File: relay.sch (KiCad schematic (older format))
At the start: 0 parts

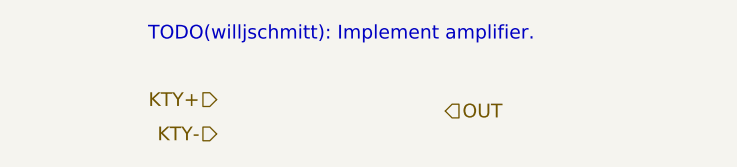
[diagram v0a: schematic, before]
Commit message: Adding contactor placeholders.
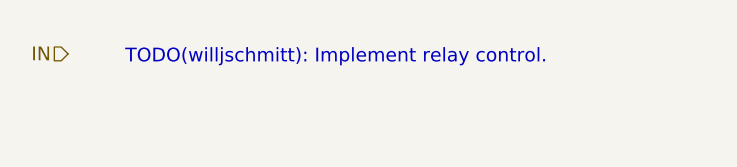
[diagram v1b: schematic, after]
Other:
- note added: "TODO(willjschmitt): Implement relay control."
- note removed: "TODO(willjschmitt): Implement amplifier."
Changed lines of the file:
@@
 $Descr A4 11693 8268
 encoding utf-8
-Sheet 13 18
+Sheet 17 18
 Title ""
 Date ""
@@
 Comment4 ""
 $EndDescr
-Text HLabel 2150 1300 0    60   Input ~ 0
-KTY+
-Text HLabel 2150 1450 0    60   Input ~ 0
-KTY-
-Text HLabel 3150 1350 2    60   Input ~ 0
-OUT
-Text Notes 1850 1050 0    60   ~ 0
-TODO(willjschmitt): Implement amplifier.
+Text HLabel 1500 1100 0    60   Input ~ 0
+IN
+Text Notes 1750 1150 0    60   ~ 0
+TODO(willjschmitt): Implement relay control.
 $EndSCHEMATC

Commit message: Implement contactor relays.
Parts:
- added D? (x2): D, symbol D
- added PRECHARGE: CONN, symbol Conn_01x02
- added Q?: Q_NPN_BCE, symbol Q_NPN_BCE
- added U?: RELAY_SPST, symbol RELAY_SPST
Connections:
- net labels added: +5V, GND
- wire segments 0 -> 16
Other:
- note removed: "TODO(willjschmitt): Implement relay control."
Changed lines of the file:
@@
 $Descr A4 11693 8268
 encoding utf-8
-Sheet 17 18
+Sheet 18 18
 Title ""
 Date ""
@@
 Comment4 ""
 $EndDescr
-Text HLabel 1500 1100 0    60   Input ~ 0
+Text HLabel 5400 4000 0    60   Input ~ 0
 IN
-Text Notes 1750 1150 0    60   ~ 0
-TODO(willjschmitt): Implement relay control.
+$Comp
+L Q_NPN_BCE Q?
+U 1 1 5B006B25
+P 5750 4000
+AR Path="/5AFF2F49/5AFF30F9/5B006B25" Ref="Q?"  Part="1"
+AR Path="/5AFF2F49/5AFF3733/5B006B25" Ref="Q?"  Part="1"
+F 0 "Q?" H 5950 4050 50  0000 L CNN
+F 1 "Q_NPN_BCE" H 5950 3950 50  0000 L CNN
+F 2 "" H 5950 4100 50  0001 C CNN
+F 3 "" H 5750 4000 50  0001 C CNN
+	1    5750 4000
+	1    0    0    -1
+$EndComp
+Wire Wire Line
+	5550 4000 5400 4000
+$Comp
+L RELAY_SPST U?
+U 1 1 5B006EB3
+P 6450 3450
+AR Path="/5AFF2F49/5AFF30F9/5B006EB3" Ref="U?"  Part="1"
+AR Path="/5AFF2F49/5AFF3733/5B006EB3" Ref="U?"  Part="1"
+F 0 "U?" H 6450 3150 60  0000 C CNN
+F 1 "RELAY_SPST" H 6450 3750 60  0000 C CNN
+F 2 "" H 6450 3450 60  0001 C CNN
+F 3 "" H 6450 3450 60  0001 C CNN
+	1    6450 3450
+	1    0    0    -1
+$EndComp
+$Comp
+L +5V #PWR?
+U 1 1 5B006F20
+P 5850 3050
+AR Path="/5AFF2F49/5AFF30F9/5B006F20" Ref="#PWR?"  Part="1"
+AR Path="/5AFF2F49/5AFF3733/5B006F20" Ref="#PWR?"  Part="1"
+F 0 "#PWR?" H 5850 2900 50  0001 C CNN
+F 1 "+5V" H 5850 3190 50  0000 C CNN
+F 2 "" H 5850 3050 50  0001 C CNN
+F 3 "" H 5850 3050 50  0001 C CNN
+	1    5850 3050
+	1    0    0    -1
+$EndComp
+$Comp
+L GND #PWR?
+U 1 1 5B006F38
+P 5850 4300
+AR Path="/5AFF2F49/5AFF30F9/5B006F38" Ref="#PWR?"  Part="1"
+AR Path="/5AFF2F49/5AFF3733/5B006F38" Ref="#PWR?"  Part="1"
+F 0 "#PWR?" H 5850 4050 50  0001 C CNN
+F 1 "GND" H 5850 4150 50  0000 C CNN
+F 2 "" H 5850 4300 50  0001 C CNN
+F 3 "" H 5850 4300 50  0001 C CNN
+	1    5850 4300
+	1    0    0    -1
+$EndComp
+$Comp
+L D D?
+U 1 1 5B006F50
+P 5700 3450
+AR Path="/5AFF2F49/5AFF30F9/5B006F50" Ref="D?"  Part="1"
+AR Path="/5AFF2F49/5AFF3733/5B006F50" Ref="D?"  Part="1"
+F 0 "D?" H 5700 3550 50  0000 C CNN
+F 1 "D" H 5700 3350 50  0000 C CNN
+F 2 "" H 5700 3450 50  0001 C CNN
+F 3 "" H 5700 3450 50  0001 C CNN
+	1    5700 3450
+	0    1    1    0
+$EndComp
+Wire Wire Line
+	5700 3300 5700 3200
+Wire Wire Line
+	5700 3200 6000 3200
+Wire Wire Line
+	6000 3200 6000 3300
+Wire Wire Line
+	5850 3050 5850 3200
+Connection ~ 5850 3200
+Wire Wire Line
+	5700 3600 5700 3700
+Wire Wire Line
+	5700 3700 6000 3700
+Wire Wire Line
+	6000 3700 6000 3600
+Wire Wire Line
+	5850 3800 5850 3700
+Connection ~ 5850 3700
+Wire Wire Line
+	5850 4200 5850 4300
+$Comp
+L D D?
+U 1 1 5B007427
+P 7050 3450
+AR Path="/5AFF2F49/5AFF30F9/5B007427" Ref="D?"  Part="1"
+AR Path="/5AFF2F49/5AFF3733/5B007427" Ref="D?"  Part="1"
+F 0 "D?" H 7050 3550 50  0000 C CNN
+F 1 "D" H 7050 3350 50  0000 C CNN
+F 2 "" H 7050 3450 50  0001 C CNN
+F 3 "" H 7050 3450 50  0001 C CNN
+	1    7050 3450
+	0    1    1    0
+$EndComp
+$Comp
+L Conn_01x02 PRECHARGE
+U 1 1 5B007450
+P 7600 3400
+AR Path="/5AFF2F49/5AFF30F9/5B007450" Ref="PRECHARGE"  Part="1"
+AR Path="/5AFF2F49/5AFF3733/5B007450" Ref="MAIN"  Part="1"
+F 0 "MAIN" H 7600 3500 50  0000 C CNN
+F 1 "CONN" H 7600 3200 50  0000 C CNN
+F 2 "" H 7600 3400 50  0001 C CNN
+F 3 "" H 7600 3400 50  0001 C CNN
+	1    7600 3400
+	1    0    0    -1
+$EndComp
+Wire Wire Line
+	6900 3300 7300 3300
+Wire Wire Line
+	7300 3300 7300 3400
+Wire Wire Line
+	7300 3400 7400 3400
+Connection ~ 7050 3300
+Wire Wire Line
+	7400 3500 7300 3500
+Wire Wire Line
+	7300 3600 7300 3500
+Wire Wire Line
+	6900 3600 7300 3600
+Connection ~ 7050 3600
 $EndSCHEMATC

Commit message: Remove extra relay and use only transistor to power contactors.
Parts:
- removed D?: D, symbol D
- removed U?: RELAY_SPST, symbol RELAY_SPST
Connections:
- wire segments 16 -> 14
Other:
- moved on the sheet: PRECHARGE
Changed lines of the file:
@@
 $Descr A4 11693 8268
 encoding utf-8
-Sheet 18 18
+Sheet 17 18
 Title ""
 Date ""
@@
 Wire Wire Line
 	5550 4000 5400 4000
-$Comp
-L RELAY_SPST U?
-U 1 1 5B006EB3
-P 6450 3450
-AR Path="/5AFF2F49/5AFF30F9/5B006EB3" Ref="U?"  Part="1"
-AR Path="/5AFF2F49/5AFF3733/5B006EB3" Ref="U?"  Part="1"
-F 0 "U?" H 6450 3150 60  0000 C CNN
-F 1 "RELAY_SPST" H 6450 3750 60  0000 C CNN
-F 2 "" H 6450 3450 60  0001 C CNN
-F 3 "" H 6450 3450 60  0001 C CNN
-	1    6450 3450
-	1    0    0    -1
-$EndComp
 $Comp
 L +5V #PWR?
@@
 	5850 4200 5850 4300
 $Comp
-L D D?
-U 1 1 5B007427
-P 7050 3450
-AR Path="/5AFF2F49/5AFF30F9/5B007427" Ref="D?"  Part="1"
-AR Path="/5AFF2F49/5AFF3733/5B007427" Ref="D?"  Part="1"
-F 0 "D?" H 7050 3550 50  0000 C CNN
-F 1 "D" H 7050 3350 50  0000 C CNN
-F 2 "" H 7050 3450 50  0001 C CNN
-F 3 "" H 7050 3450 50  0001 C CNN
-	1    7050 3450
-	0    1    1    0
-$EndComp
-$Comp
 L Conn_01x02 PRECHARGE
 U 1 1 5B007450
-P 7600 3400
+P 6300 3400
 AR Path="/5AFF2F49/5AFF30F9/5B007450" Ref="PRECHARGE"  Part="1"
 AR Path="/5AFF2F49/5AFF3733/5B007450" Ref="MAIN"  Part="1"
-F 0 "MAIN" H 7600 3500 50  0000 C CNN
-F 1 "CONN" H 7600 3200 50  0000 C CNN
-F 2 "" H 7600 3400 50  0001 C CNN
-F 3 "" H 7600 3400 50  0001 C CNN
-	1    7600 3400
+F 0 "PRECHARGE" H 6300 3500 50  0000 C CNN
+F 1 "CONN" H 6300 3200 50  0000 C CNN
+F 2 "" H 6300 3400 50  0001 C CNN
+F 3 "" H 6300 3400 50  0001 C CNN
+	1    6300 3400
 	1    0    0    -1
 $EndComp
 Wire Wire Line
-	6900 3300 7300 3300
+	6000 3300 6000 3400
 Wire Wire Line
-	7300 3300 7300 3400
+	6000 3400 6100 3400
 Wire Wire Line
-	7300 3400 7400 3400
-Connection ~ 7050 3300
+	6100 3500 6000 3500
 Wire Wire Line
-	7400 3500 7300 3500
-Wire Wire Line
-	7300 3600 7300 3500
-Wire Wire Line
-	6900 3600 7300 3600
-Connection ~ 7050 3600
+	6000 3600 6000 3500
 $EndSCHEMATC

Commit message: Annotate and add negative IOC faults.
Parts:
- gave numbers to parts that had none: 2
- renumbered PRECHARGE to PRECHARGE1
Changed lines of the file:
@@
 $Descr A4 11693 8268
 encoding utf-8
-Sheet 17 19
+Sheet 18 19
 Title ""
 Date ""
@@
 IN
 $Comp
-L Q_NPN_BCE Q?
+L Q_NPN_BCE Q1
 U 1 1 5B006B25
 P 5750 4000
-AR Path="/5AFF2F49/5AFF30F9/5B006B25" Ref="Q?"  Part="1"
-AR Path="/5AFF2F49/5AFF3733/5B006B25" Ref="Q?"  Part="1"
-F 0 "Q?" H 5950 4050 50  0000 L CNN
+AR Path="/5AFF2F49/5AFF30F9/5B006B25" Ref="Q1"  Part="1"
+AR Path="/5AFF2F49/5AFF3733/5B006B25" Ref="Q2"  Part="1"
+F 0 "Q2" H 5950 4050 50  0000 L CNN
 F 1 "Q_NPN_BCE" H 5950 3950 50  0000 L CNN
 F 2 "" H 5950 4100 50  0001 C CNN
@@
 	5550 4000 5400 4000
 $Comp
-L +5V #PWR?
+L +5V #PWR81
 U 1 1 5B006F20
 P 5850 3050
-AR Path="/5AFF2F49/5AFF30F9/5B006F20" Ref="#PWR?"  Part="1"
-AR Path="/5AFF2F49/5AFF3733/5B006F20" Ref="#PWR?"  Part="1"
-F 0 "#PWR?" H 5850 2900 50  0001 C CNN
+AR Path="/5AFF2F49/5AFF30F9/5B006F20" Ref="#PWR81"  Part="1"
+AR Path="/5AFF2F49/5AFF3733/5B006F20" Ref="#PWR83"  Part="1"
+F 0 "#PWR83" H 5850 2900 50  0001 C CNN
 F 1 "+5V" H 5850 3190 50  0000 C CNN
 F 2 "" H 5850 3050 50  0001 C CNN
@@
 $EndComp
 $Comp
-L GND #PWR?
+L GND #PWR82
 U 1 1 5B006F38
 P 5850 4300
-AR Path="/5AFF2F49/5AFF30F9/5B006F38" Ref="#PWR?"  Part="1"
-AR Path="/5AFF2F49/5AFF3733/5B006F38" Ref="#PWR?"  Part="1"
-F 0 "#PWR?" H 5850 4050 50  0001 C CNN
+AR Path="/5AFF2F49/5AFF30F9/5B006F38" Ref="#PWR82"  Part="1"
+AR Path="/5AFF2F49/5AFF3733/5B006F38" Ref="#PWR84"  Part="1"
+F 0 "#PWR84" H 5850 4050 50  0001 C CNN
 F 1 "GND" H 5850 4150 50  0000 C CNN
 F 2 "" H 5850 4300 50  0001 C CNN
@@
 $EndComp
 $Comp
-L D D?
+L D D1
 U 1 1 5B006F50
 P 5700 3450
-AR Path="/5AFF2F49/5AFF30F9/5B006F50" Ref="D?"  Part="1"
-AR Path="/5AFF2F49/5AFF3733/5B006F50" Ref="D?"  Part="1"
-F 0 "D?" H 5700 3550 50  0000 C CNN
+AR Path="/5AFF2F49/5AFF30F9/5B006F50" Ref="D1"  Part="1"
+AR Path="/5AFF2F49/5AFF3733/5B006F50" Ref="D2"  Part="1"
+F 0 "D2" H 5700 3550 50  0000 C CNN
 F 1 "D" H 5700 3350 50  0000 C CNN
 F 2 "" H 5700 3450 50  0001 C CNN
@@
 	5700 3200 6000 3200
 Wire Wire Line
-	6000 3200 6000 3300
+	6000 3200 6000 3400
 Wire Wire Line
 	5850 3050 5850 3200
@@
 	5700 3600 5700 3700
 Wire Wire Line
-	5700 3700 6000 3700
+	6000 3700 5700 3700
 Wire Wire Line
-	6000 3700 6000 3600
+	6000 3500 6000 3700
 Wire Wire Line
 	5850 3800 5850 3700
@@
 	5850 4200 5850 4300
 $Comp
-L Conn_01x02 PRECHARGE
+L Conn_01x02 PRECHARGE1
 U 1 1 5B007450
 P 6300 3400
-AR Path="/5AFF2F49/5AFF30F9/5B007450" Ref="PRECHARGE"  Part="1"
-AR Path="/5AFF2F49/5AFF3733/5B007450" Ref="MAIN"  Part="1"
-F 0 "PRECHARGE" H 6300 3500 50  0000 C CNN
+AR Path="/5AFF2F49/5AFF30F9/5B007450" Ref="PRECHARGE1"  Part="1"
+AR Path="/5AFF2F49/5AFF3733/5B007450" Ref="MAIN1"  Part="1"
+F 0 "MAIN1" H 6300 3500 50  0000 C CNN
 F 1 "CONN" H 6300 3200 50  0000 C CNN
 F 2 "" H 6300 3400 50  0001 C CNN
@@
 $EndComp
 Wire Wire Line
-	6000 3300 6000 3400
-Wire Wire Line
 	6000 3400 6100 3400
 Wire Wire Line
 	6100 3500 6000 3500
-Wire Wire Line
-	6000 3600 6000 3500
 $EndSCHEMATC

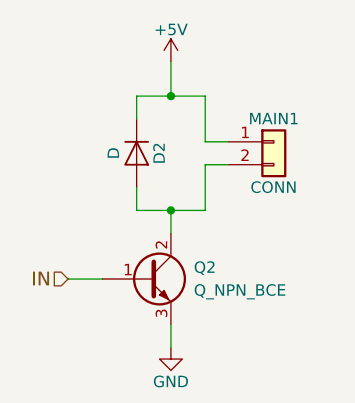
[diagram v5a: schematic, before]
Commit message: Adds IOC reference points.
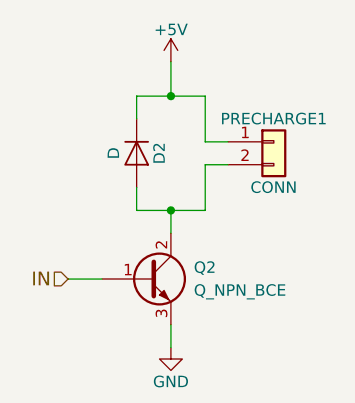
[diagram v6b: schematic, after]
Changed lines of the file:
@@
 	5550 4000 5400 4000
 $Comp
-L +5V #PWR81
+L +5V #PWR85
 U 1 1 5B006F20
 P 5850 3050
-AR Path="/5AFF2F49/5AFF30F9/5B006F20" Ref="#PWR81"  Part="1"
-AR Path="/5AFF2F49/5AFF3733/5B006F20" Ref="#PWR83"  Part="1"
-F 0 "#PWR83" H 5850 2900 50  0001 C CNN
+AR Path="/5AFF2F49/5AFF30F9/5B006F20" Ref="#PWR85"  Part="1"
+AR Path="/5AFF2F49/5AFF3733/5B006F20" Ref="#PWR87"  Part="1"
+F 0 "#PWR87" H 5850 2900 50  0001 C CNN
 F 1 "+5V" H 5850 3190 50  0000 C CNN
 F 2 "" H 5850 3050 50  0001 C CNN
@@
 $EndComp
 $Comp
-L GND #PWR82
+L GND #PWR86
 U 1 1 5B006F38
 P 5850 4300
-AR Path="/5AFF2F49/5AFF30F9/5B006F38" Ref="#PWR82"  Part="1"
-AR Path="/5AFF2F49/5AFF3733/5B006F38" Ref="#PWR84"  Part="1"
-F 0 "#PWR84" H 5850 4050 50  0001 C CNN
+AR Path="/5AFF2F49/5AFF30F9/5B006F38" Ref="#PWR86"  Part="1"
+AR Path="/5AFF2F49/5AFF3733/5B006F38" Ref="#PWR88"  Part="1"
+F 0 "#PWR88" H 5850 4050 50  0001 C CNN
 F 1 "GND" H 5850 4150 50  0000 C CNN
 F 2 "" H 5850 4300 50  0001 C CNN
@@
 AR Path="/5AFF2F49/5AFF30F9/5B007450" Ref="PRECHARGE1"  Part="1"
 AR Path="/5AFF2F49/5AFF3733/5B007450" Ref="MAIN1"  Part="1"
-F 0 "MAIN1" H 6300 3500 50  0000 C CNN
+F 0 "PRECHARGE1" H 6300 3500 50  0000 C CNN
 F 1 "CONN" H 6300 3200 50  0000 C CNN
 F 2 "" H 6300 3400 50  0001 C CNN
